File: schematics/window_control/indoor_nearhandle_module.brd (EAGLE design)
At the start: 39.4 x 83.5 mm, 19 parts, among them J1 J2, J2 J2, Q1 2N3904, SW1 MRS-101-2C3-B, U1 ESP32, U4 SN74LS32N

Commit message: Connectors changed
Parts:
- removed J2: J2, my_devices:J2
- J1: value J2 -> JST-XH2.54-4P; device my_devices:J2 -> my_devices:JST-XH254-4P
- moved J1 5.24 mm to (34.3, 68.6), turned to 0 degrees
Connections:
- net +5V: now also J1.PIN2; no longer J2.PIN_1
- net GND: now also J1.PIN1; no longer J2.PIN_2
- net OUTDOOR_SIGNAL: now also J1.PIN4; no longer J1.PIN_2
- net SERVO_PWM_CONTROL: now also J1.PIN3; no longer J1.PIN_1
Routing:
- net SERVO_PWM_CONTROL: track 62.4 -> 50.1 mm
- net GND: track 185.4 -> 189.7 mm
- net +5V: track 128.1 -> 127.4 mm
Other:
- board text removed: "+5V"
- board text removed: "J1"
- board text removed: "J2"
- board text removed: "OUT_SGN"
- board text removed: "SRV_PWM"
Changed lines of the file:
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@@
 <drawing>
 <settings>
-<setting alwaysvectorfont="yes"/>
+<setting alwaysvectorfont="no"/>
 <setting verticaltext="up"/>
 </settings>
@@
 <text x="16.51" y="73.66" size="0.8128" layer="25">SB2</text>
 <text x="50.8" y="73.66" size="0.8128" layer="25">SB1</text>
-<text x="24.13" y="63.5" size="1.778" layer="25">J2</text>
-<text x="43.18" y="63.5" size="1.778" layer="25">J1</text>
 <text x="38.1" y="59.69" size="1.778" layer="25">R8</text>
 <text x="27.94" y="58.42" size="1.778" layer="25">R5</text>
@@
 <text x="44.45" y="6.35" size="1.778" layer="25">SW1</text>
 <text x="39.37" y="-2.54" size="1.778" layer="25">B1</text>
-<text x="29.21" y="66.04" size="1.778" layer="26" rot="MR0">GND</text>
-<text x="33.02" y="72.39" size="1.778" layer="26" rot="MR0">+5V</text>
-<text x="43.18" y="66.04" size="1.778" layer="26" rot="MR0">OUT_SGN</text>
-<text x="48.26" y="72.39" size="1.778" layer="26" rot="MR0">SRV_PWM</text>
+<text x="29.21" y="67.31" size="1.778" layer="26" rot="MR0">GND</text>
 </plain>
 <attributes>
@@
 <element name="B1" library="my_devices" package="HALL_SENSOR" value="A3144" x="34.29" y="-2.54" smashed="yes" rot="R90"/>
 <element name="D1" library="my_devices" package="LD" value="GNL-3014ED" x="34.29" y="3.81" smashed="yes" rot="R180"/>
-<element name="J1" library="my_devices" package="J2" value="J2" x="39.37" y="69.85" smashed="yes" rot="R270"/>
-<element name="J2" library="my_devices" package="J2" value="J2" x="29.21" y="69.85" smashed="yes" rot="R270"/>
 <element name="Q1" library="my_devices" package="TRANSISTOR" value="2N3904" x="24.13" y="5.08" smashed="yes" rot="R270"/>
 <element name="R1" library="my_devices" package="R" value="620" x="27.94" y="33.02" smashed="yes" rot="R270">
@@
 </element>
 <element name="U4" library="my_devices" package="DIP14" value="SN74LS32N" x="38.1" y="30.48" smashed="yes"/>
+<element name="J1" library="my_devices" package="JST-XH254-4P" value="JST-XH2.54-4P" x="34.29" y="68.58" smashed="yes">
+<attribute name="NAME" x="41.91" y="68.58" size="1.27" layer="21"/>
+</element>
 </elements>
 <signals>
@@
 <contactref element="B1" pad="VCC"/>
 <contactref element="R2" pad="P$2"/>
-<contactref element="J2" pad="PIN_1"/>
 <contactref element="U1" pad="+5V"/>
 <wire x1="19.05" y1="13.97" x2="19.05" y2="58.42" width="1.016" layer="16"/>
@@
 <wire x1="41.91" y1="38.1" x2="30.48" y2="49.53" width="1.016" layer="16"/>
 <wire x1="30.48" y1="49.53" x2="30.48" y2="59.69" width="1.016" layer="16"/>
-<wire x1="30.48" y1="59.69" x2="30.48" y2="62.23" width="1.016" layer="16"/>
-<wire x1="30.48" y1="62.23" x2="30.48" y2="63.5" width="1.016" layer="16"/>
 <wire x1="31.75" y1="-2.54" x2="26.67" y2="-2.54" width="1.016" layer="16"/>
 <wire x1="26.67" y1="-2.54" x2="19.05" y2="5.08" width="1.016" layer="16"/>
@@
 <wire x1="19.05" y1="58.42" x2="20.32" y2="59.69" width="1.016" layer="16"/>
 <wire x1="20.32" y1="59.69" x2="30.48" y2="59.69" width="1.016" layer="16"/>
-<wire x1="30.48" y1="63.5" x2="30.48" y2="68.58" width="1.016" layer="16"/>
-<wire x1="30.48" y1="68.58" x2="31.75" y2="69.85" width="1.016" layer="16"/>
+<contactref element="J1" pad="PIN2"/>
+<wire x1="30.48" y1="59.69" x2="33.02" y2="62.23" width="1.016" layer="16"/>
+<wire x1="33.02" y1="62.23" x2="33.02" y2="68.58" width="1.016" layer="16"/>
 </signal>
 <signal name="GND">
@@
 <contactref element="SB2" pad="B"/>
 <contactref element="SB1" pad="B"/>
-<contactref element="J2" pad="PIN_2"/>
 <contactref element="U1" pad="GND"/>
 <contactref element="R6" pad="P1"/>
@@
 <wire x1="53.066" y1="59.416" x2="50.8" y2="57.15" width="1.016" layer="16"/>
 <wire x1="53.066" y1="67.33" x2="53.066" y2="59.416" width="1.016" layer="16"/>
-<wire x1="24.13" y1="70.104" x2="24.424" y2="69.81" width="1.016" layer="16"/>
-<wire x1="24.424" y1="69.81" x2="26.71" y2="69.81" width="1.016" layer="16"/>
 <polygon width="0.1524" layer="16" isolate="0.4064">
 <vertex x="16.51" y="77.47"/>
@@
 <vertex x="16.51" y="-3.81"/>
 </polygon>
+<contactref element="J1" pad="PIN1"/>
+<wire x1="24.13" y1="70.104" x2="28.956" y2="70.104" width="1.016" layer="16"/>
+<wire x1="28.956" y1="70.104" x2="30.48" y2="68.58" width="1.016" layer="16"/>
 </signal>
 <signal name="GPIO_TS_WINDOW_OPEN">
@@
 <signal name="SERVO_PWM_CONTROL">
 <contactref element="U4" pad="PIN_8"/>
-<contactref element="J1" pad="PIN_1"/>
 <wire x1="41.91" y1="22.86" x2="43.18" y2="24.13" width="0.508" layer="1"/>
 <wire x1="43.18" y1="49.53" x2="41.91" y2="50.8" width="0.508" layer="1"/>
 <wire x1="41.91" y1="50.8" x2="40.64" y2="50.8" width="0.508" layer="1"/>
 <wire x1="43.18" y1="24.13" x2="43.18" y2="49.53" width="0.508" layer="1"/>
-<wire x1="34.29" y1="71.12" x2="35.56" y2="72.39" width="0.508" layer="1"/>
-<wire x1="35.56" y1="72.39" x2="39.37" y2="72.39" width="0.508" layer="1"/>
-<wire x1="39.37" y1="72.39" x2="41.91" y2="69.85" width="0.508" layer="1"/>
-<wire x1="40.64" y1="50.8" x2="34.29" y2="57.15" width="0.508" layer="1"/>
-<wire x1="34.29" y1="57.15" x2="34.29" y2="71.12" width="0.508" layer="1"/>
+<contactref element="J1" pad="PIN3"/>
+<wire x1="40.64" y1="50.8" x2="35.56" y2="55.88" width="0.508" layer="1"/>
+<wire x1="35.56" y1="55.88" x2="35.56" y2="68.58" width="0.508" layer="1"/>
 </signal>
 <signal name="N$3">
@@
 </signal>
 <signal name="OUTDOOR_SIGNAL">
-<contactref element="J1" pad="PIN_2"/>
 <contactref element="R6" pad="P2"/>
-<wire x1="44.45" y1="51.4572625" x2="38.42863125" y2="57.47863125" width="0.508" layer="1"/>
-<wire x1="38.42863125" y1="57.47863125" x2="38.1" y2="57.8072625" width="0.508" layer="1"/>
 <wire x1="40.64" y1="15.24" x2="40.64" y2="19.05" width="0.508" layer="1"/>
-<wire x1="44.45" y1="22.86" x2="44.45" y2="51.4572625" width="0.508" layer="1"/>
+<wire x1="44.45" y1="22.86" x2="44.45" y2="50.8" width="0.508" layer="1"/>
+<wire x1="44.45" y1="50.8" x2="44.45" y2="51.4572625" width="0.508" layer="1"/>
 <wire x1="40.64" y1="19.05" x2="44.45" y2="22.86" width="0.508" layer="1"/>
-<wire x1="38.42863125" y1="57.47863125" x2="38.42863125" y2="68.25136875" width="0.508" layer="1"/>
-<wire x1="38.42863125" y1="68.25136875" x2="36.87" y2="69.81" width="0.508" layer="1"/>
+<contactref element="J1" pad="PIN4"/>
+<wire x1="44.45" y1="51.4572625" x2="44.45" y2="53.34" width="0.508" layer="1"/>
+<wire x1="44.45" y1="53.34" x2="43.18" y2="54.61" width="0.508" layer="1"/>
+<wire x1="43.18" y1="54.61" x2="39.37" y2="54.61" width="0.508" layer="1"/>
+<wire x1="39.37" y1="54.61" x2="38.1" y2="55.88" width="0.508" layer="1"/>
+<wire x1="38.1" y1="55.88" x2="38.1" y2="68.58" width="0.508" layer="1"/>
 </signal>
 <signal name="N$6">

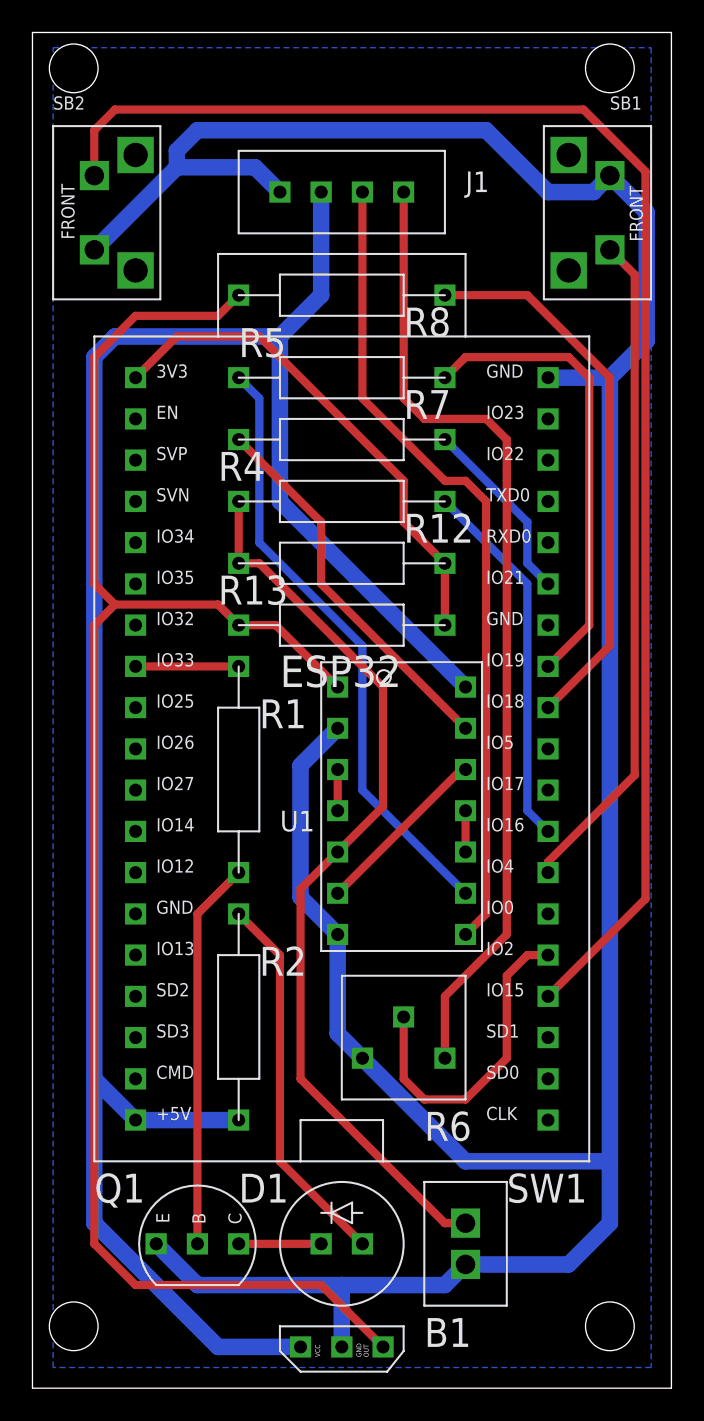
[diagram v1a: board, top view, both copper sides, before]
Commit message: Outdoor module board size reduced
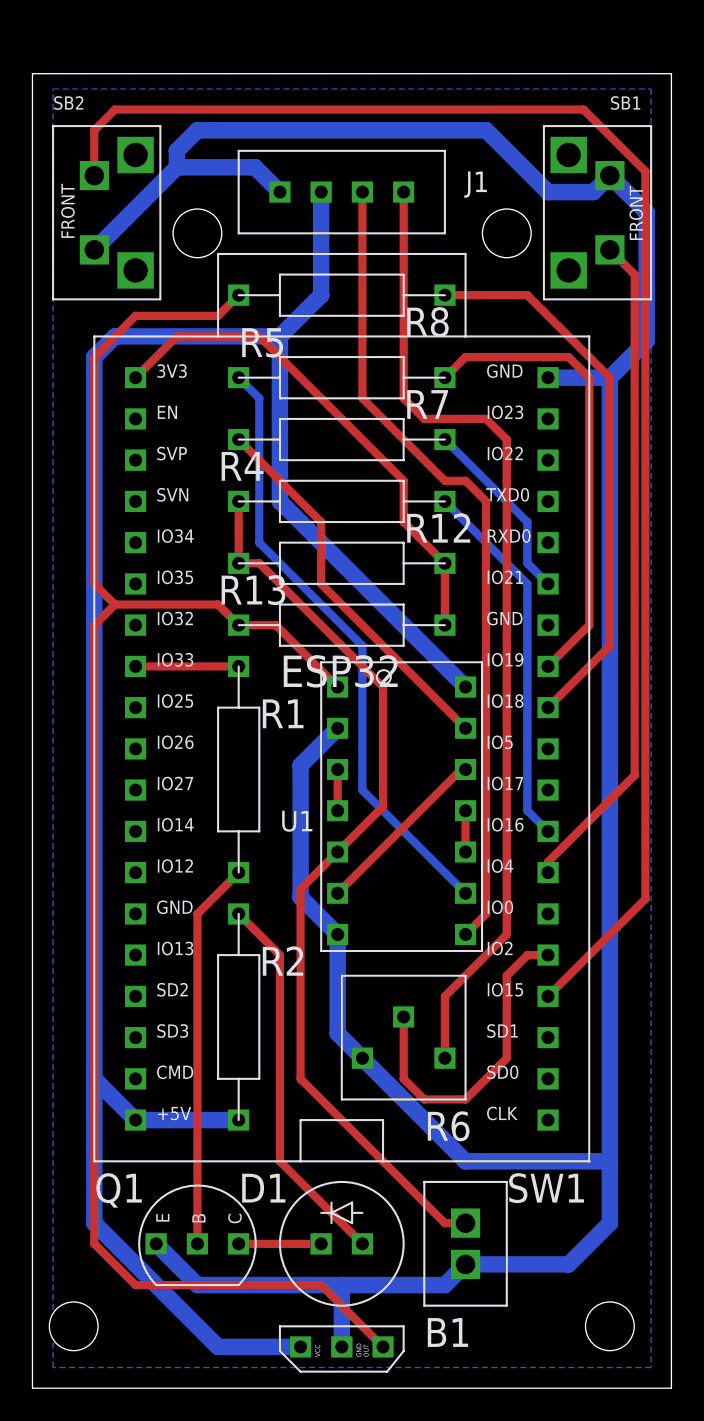
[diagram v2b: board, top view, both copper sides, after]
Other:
- board size 39.4 x 83.5 mm -> 39.4 x 81 mm
- board text added: "+5V"
- board text added: "PWM"
- board text added: "SGN"
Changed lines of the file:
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@@
 <plain>
 <wire x1="15.24" y1="-5.08" x2="54.59" y2="-5.08" width="0" layer="20"/>
-<wire x1="54.59" y1="-5.08" x2="54.59" y2="78.41" width="0" layer="20"/>
-<wire x1="54.59" y1="78.41" x2="15.24" y2="78.41" width="0" layer="20"/>
-<wire x1="15.24" y1="78.41" x2="15.24" y2="-5.08" width="0" layer="20"/>
-<hole x="50.8" y="76.2" drill="3"/>
-<hole x="17.78" y="76.2" drill="3"/>
+<wire x1="54.59" y1="-5.08" x2="54.59" y2="75.87" width="0" layer="20"/>
+<wire x1="54.59" y1="75.87" x2="15.24" y2="75.87" width="0" layer="20"/>
+<wire x1="15.24" y1="75.87" x2="15.24" y2="-5.08" width="0" layer="20"/>
+<hole x="44.45" y="66.04" drill="3"/>
+<hole x="25.4" y="66.04" drill="3"/>
 <hole x="17.78" y="-1.27" drill="3"/>
 <hole x="50.8" y="-1.27" drill="3"/>
@@
 <text x="44.45" y="6.35" size="1.778" layer="25">SW1</text>
 <text x="39.37" y="-2.54" size="1.778" layer="25">B1</text>
-<text x="29.21" y="67.31" size="1.778" layer="26" rot="MR0">GND</text>
+<text x="30.48" y="69.85" size="1.778" layer="26" rot="MR0">GND</text>
+<text x="34.29" y="66.04" size="1.778" layer="26" rot="MR0">+5V</text>
+<text x="38.1" y="69.85" size="1.778" layer="26" rot="MR0">PWM</text>
+<text x="41.91" y="66.04" size="1.778" layer="26" rot="MR0">SGN</text>
 </plain>
 <attributes>
@@
 <wire x1="53.066" y1="67.33" x2="53.066" y2="59.416" width="1.016" layer="16"/>
 <polygon width="0.1524" layer="16" isolate="0.4064">
-<vertex x="16.51" y="77.47"/>
-<vertex x="53.34" y="77.47"/>
+<vertex x="16.51" y="74.93"/>
+<vertex x="53.34" y="74.93"/>
 <vertex x="53.34" y="-3.81"/>
 <vertex x="16.51" y="-3.81"/>

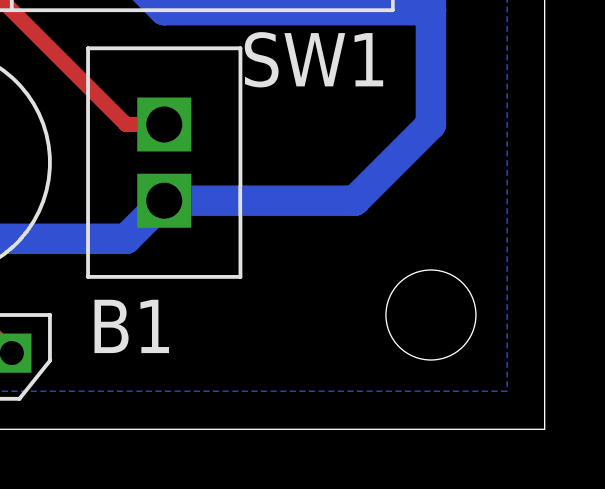
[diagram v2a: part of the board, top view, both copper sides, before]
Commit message: Start preparing to order boards. Checked all labels
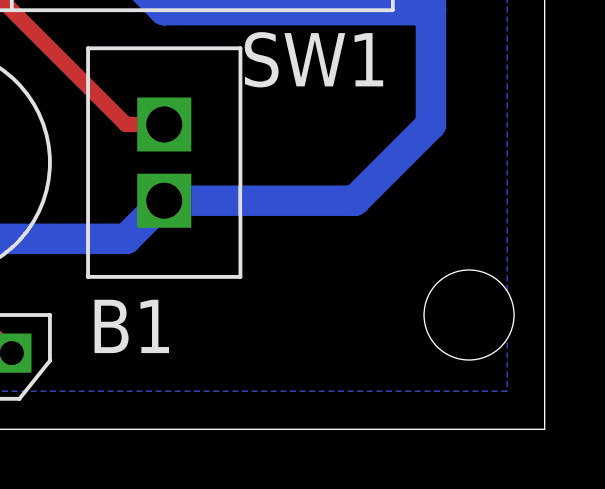
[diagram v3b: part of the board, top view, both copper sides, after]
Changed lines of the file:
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@@
 <drawing>
 <settings>
-<setting alwaysvectorfont="no"/>
+<setting alwaysvectorfont="yes"/>
 <setting verticaltext="up"/>
 </settings>
@@
 <hole x="25.4" y="66.04" drill="3"/>
 <hole x="17.78" y="-1.27" drill="3"/>
-<hole x="50.8" y="-1.27" drill="3"/>
+<hole x="52.07" y="-1.27" drill="3"/>
 <text x="16.51" y="73.66" size="0.8128" layer="25">SB2</text>
 <text x="50.8" y="73.66" size="0.8128" layer="25">SB1</text>

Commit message: Boards checked and ready to order
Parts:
- moved J1 1.27 mm to (34.3, 69.8)
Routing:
- net +5V: track 127.4 -> 128.6 mm
- net SERVO_PWM_CONTROL: track 50.1 -> 51.4 mm
- net OUTDOOR_SIGNAL: track 59.8 -> 61.1 mm
- net 3V3: track 31.2 -> 30.4 mm
- net GND: track 189.7 -> 189.1 mm
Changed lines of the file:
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@@
 <drawing>
 <settings>
-<setting alwaysvectorfont="yes"/>
+<setting alwaysvectorfont="no"/>
 <setting verticaltext="up"/>
 </settings>
@@
 <text x="44.45" y="6.35" size="1.778" layer="25">SW1</text>
 <text x="39.37" y="-2.54" size="1.778" layer="25">B1</text>
-<text x="30.48" y="69.85" size="1.778" layer="26" rot="MR0">GND</text>
-<text x="34.29" y="66.04" size="1.778" layer="26" rot="MR0">+5V</text>
-<text x="38.1" y="69.85" size="1.778" layer="26" rot="MR0">PWM</text>
-<text x="41.91" y="66.04" size="1.778" layer="26" rot="MR0">SGN</text>
+<text x="30.48" y="71.12" size="1.778" layer="26" rot="MR0">GND</text>
+<text x="34.29" y="67.31" size="1.778" layer="26" rot="MR0">+5V</text>
+<text x="38.1" y="71.12" size="1.778" layer="26" rot="MR0">PWM</text>
+<text x="41.91" y="67.31" size="1.778" layer="26" rot="MR0">SGN</text>
 </plain>
 <attributes>
@@
 </element>
 <element name="U4" library="my_devices" package="DIP14" value="SN74LS32N" x="38.1" y="30.48" smashed="yes"/>
-<element name="J1" library="my_devices" package="JST-XH254-4P" value="JST-XH2.54-4P" x="34.29" y="68.58" smashed="yes">
-<attribute name="NAME" x="41.91" y="68.58" size="1.27" layer="21"/>
+<element name="J1" library="my_devices" package="JST-XH254-4P" value="JST-XH2.54-4P" x="34.29" y="69.85" smashed="yes">
+<attribute name="NAME" x="41.91" y="69.85" size="1.27" layer="21"/>
 </element>
 </elements>
@@
 <contactref element="J1" pad="PIN2"/>
 <wire x1="30.48" y1="59.69" x2="33.02" y2="62.23" width="1.016" layer="16"/>
-<wire x1="33.02" y1="62.23" x2="33.02" y2="68.58" width="1.016" layer="16"/>
+<wire x1="33.02" y1="62.23" x2="33.02" y2="69.85" width="1.016" layer="16"/>
 </signal>
 <signal name="GND">
@@
 </polygon>
 <contactref element="J1" pad="PIN1"/>
-<wire x1="24.13" y1="70.104" x2="28.956" y2="70.104" width="1.016" layer="16"/>
-<wire x1="28.956" y1="70.104" x2="30.48" y2="68.58" width="1.016" layer="16"/>
+<wire x1="24.13" y1="70.104" x2="30.226" y2="70.104" width="1.016" layer="16"/>
+<wire x1="30.226" y1="70.104" x2="30.48" y2="69.85" width="1.016" layer="16"/>
 </signal>
 <signal name="GPIO_TS_WINDOW_OPEN">
@@
 <contactref element="J1" pad="PIN3"/>
 <wire x1="40.64" y1="50.8" x2="35.56" y2="55.88" width="0.508" layer="1"/>
-<wire x1="35.56" y1="55.88" x2="35.56" y2="68.58" width="0.508" layer="1"/>
+<wire x1="35.56" y1="55.88" x2="35.56" y2="69.85" width="0.508" layer="1"/>
 </signal>
 <signal name="N$3">
@@
 <contactref element="R12" pad="P$1"/>
 <contactref element="U1" pad="3V3"/>
-<wire x1="21.59" y1="57.15" x2="24.13" y2="59.69" width="0.508" layer="1"/>
-<wire x1="24.13" y1="59.69" x2="29.21" y2="59.69" width="0.508" layer="1"/>
-<wire x1="29.21" y1="59.69" x2="38.1" y2="50.8" width="0.508" layer="1"/>
-<wire x1="38.1" y1="50.8" x2="38.1" y2="48.26" width="0.508" layer="1"/>
-<wire x1="38.1" y1="48.26" x2="40.64" y2="45.72" width="0.508" layer="1"/>
-<wire x1="40.64" y1="45.72" x2="40.64" y2="41.91" width="0.508" layer="1"/>
+<wire x1="21.59" y1="57.15" x2="24.13" y2="59.69" width="1.016" layer="1"/>
+<wire x1="40.64" y1="46.99" x2="40.64" y2="45.72" width="1.016" layer="1"/>
+<wire x1="24.13" y1="59.69" x2="27.94" y2="59.69" width="1.016" layer="1"/>
+<wire x1="27.94" y1="59.69" x2="40.64" y2="46.99" width="1.016" layer="1"/>
+<wire x1="40.64" y1="45.72" x2="40.64" y2="41.91" width="1.016" layer="1"/>
 </signal>
 <signal name="N$56">
@@
 <contactref element="R6" pad="P2"/>
 <wire x1="40.64" y1="15.24" x2="40.64" y2="19.05" width="0.508" layer="1"/>
-<wire x1="44.45" y1="22.86" x2="44.45" y2="50.8" width="0.508" layer="1"/>
-<wire x1="44.45" y1="50.8" x2="44.45" y2="51.4572625" width="0.508" layer="1"/>
+<wire x1="44.45" y1="22.86" x2="44.45" y2="53.34" width="0.508" layer="1"/>
 <wire x1="40.64" y1="19.05" x2="44.45" y2="22.86" width="0.508" layer="1"/>
 <contactref element="J1" pad="PIN4"/>
-<wire x1="44.45" y1="51.4572625" x2="44.45" y2="53.34" width="0.508" layer="1"/>
 <wire x1="44.45" y1="53.34" x2="43.18" y2="54.61" width="0.508" layer="1"/>
 <wire x1="43.18" y1="54.61" x2="39.37" y2="54.61" width="0.508" layer="1"/>
 <wire x1="39.37" y1="54.61" x2="38.1" y2="55.88" width="0.508" layer="1"/>
-<wire x1="38.1" y1="55.88" x2="38.1" y2="68.58" width="0.508" layer="1"/>
+<wire x1="38.1" y1="55.88" x2="38.1" y2="69.85" width="0.508" layer="1"/>
 </signal>
 <signal name="N$6">

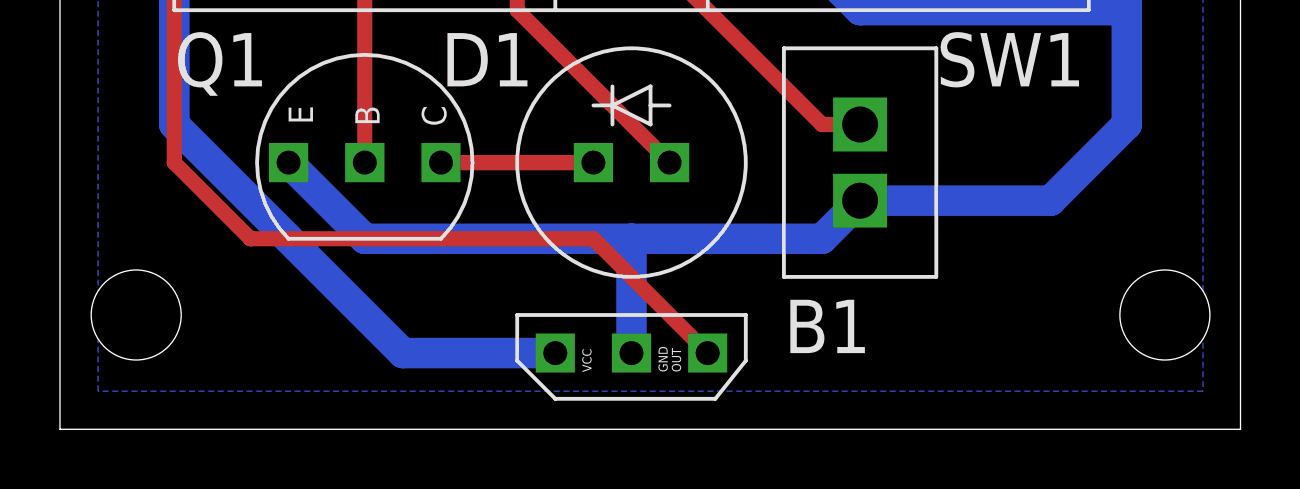
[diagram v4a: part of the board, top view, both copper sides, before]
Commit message: Holes moved away from board border
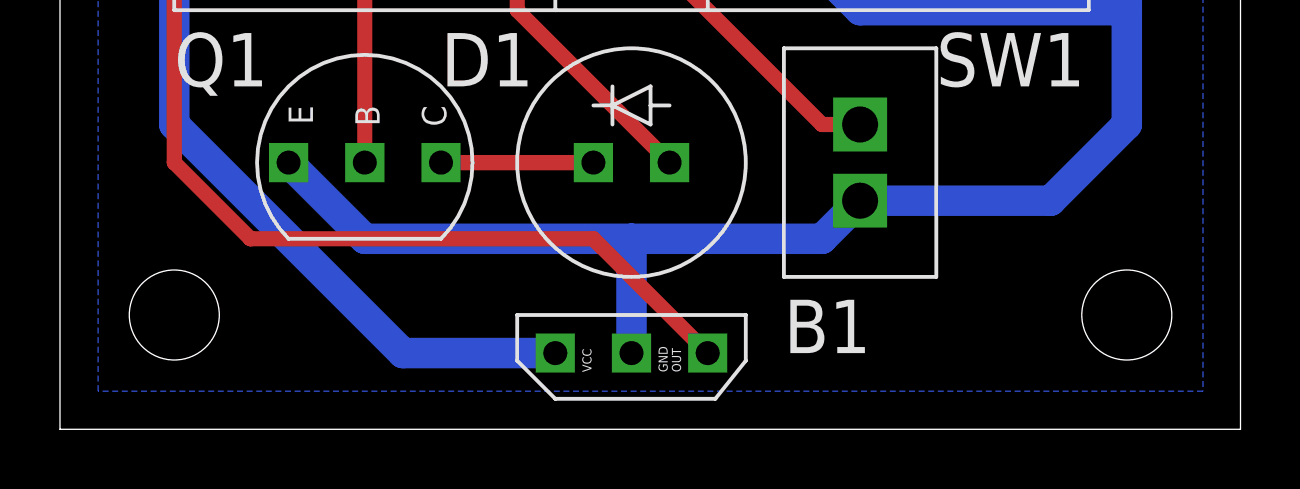
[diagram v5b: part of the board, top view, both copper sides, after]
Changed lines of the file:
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@@
 <hole x="44.45" y="66.04" drill="3"/>
 <hole x="25.4" y="66.04" drill="3"/>
-<hole x="17.78" y="-1.27" drill="3"/>
-<hole x="52.07" y="-1.27" drill="3"/>
+<hole x="19.05" y="-1.27" drill="3"/>
+<hole x="50.8" y="-1.27" drill="3"/>
 <text x="16.51" y="73.66" size="0.8128" layer="25">SB2</text>
 <text x="50.8" y="73.66" size="0.8128" layer="25">SB1</text>
